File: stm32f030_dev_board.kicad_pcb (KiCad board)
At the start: 2 copper layers, 0 parts

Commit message: Started PCB layout and added net labels to schematic
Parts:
- added C1: 100n, Capacitor_SMD:C_0402_1005Metric_Pad0.74x0.62mm_HandSolder, F.Cu at (66.1, 77.5)
- added C10: 22u, Capacitor_Tantalum_SMD:CP_EIA-3216-18_Kemet-A_Pad1.58x1.35mm_HandSolder, F.Cu at (139.4, 82.2)
- added C11: 10n, Capacitor_SMD:C_0402_1005Metric_Pad0.74x0.62mm_HandSolder, F.Cu at (147.2, 95.7)
- added C12: 100n, Capacitor_SMD:C_0402_1005Metric_Pad0.74x0.62mm_HandSolder, F.Cu at (147.2, 97.7)
- added C13: 100n, Capacitor_SMD:C_0402_1005Metric_Pad0.74x0.62mm_HandSolder, F.Cu at (150.4, 89.8)
- added C14: 100n, Capacitor_SMD:C_0402_1005Metric_Pad0.74x0.62mm_HandSolder, F.Cu at (98.9, 140.1)
- added C15: 100n, Capacitor_SMD:C_0402_1005Metric_Pad0.74x0.62mm_HandSolder, F.Cu at (90.7, 136.5)
- added C16: 100n, Capacitor_SMD:C_0402_1005Metric_Pad0.74x0.62mm_HandSolder, F.Cu at (94.4, 128.2)
- added C17: 100n, Capacitor_SMD:C_0402_1005Metric_Pad0.74x0.62mm_HandSolder, F.Cu at (150.4, 97.7)
- added C18: 100n, Capacitor_SMD:C_0402_1005Metric_Pad0.74x0.62mm_HandSolder, F.Cu at (153.6, 89.8)
- added C19: 4.7u, Capacitor_Tantalum_SMD:CP_EIA-3216-18_Kemet-A_Pad1.58x1.35mm_HandSolder, F.Cu at (139.4, 85.4)
- added C2: 100n, Capacitor_SMD:C_0402_1005Metric_Pad0.74x0.62mm_HandSolder, F.Cu at (144.0, 91.8)
- added C20: 4.7u, Capacitor_Tantalum_SMD:CP_EIA-3216-18_Kemet-A_Pad1.58x1.35mm_HandSolder, F.Cu at (139.4, 88.5)
- added C21: 27p, Capacitor_SMD:C_0402_1005Metric_Pad0.74x0.62mm_HandSolder, F.Cu at (85.1, 130.4)
- added C22: 27p, Capacitor_SMD:C_0402_1005Metric_Pad0.74x0.62mm_HandSolder, F.Cu at (85.1, 133.9)
- added C23: 20p, Capacitor_SMD:C_0603_1608Metric_Pad1.08x0.95mm_HandSolder, F.Cu at (70.3, 93.2)
- added C24: 20p, Capacitor_SMD:C_0603_1608Metric_Pad1.08x0.95mm_HandSolder, F.Cu at (70.3, 97.8)
- added C25: 4.7u, Capacitor_Tantalum_SMD:CP_EIA-3216-18_Kemet-A_Pad1.58x1.35mm_HandSolder, F.Cu at (139.4, 91.7)
- added C26: 6p, Capacitor_SMD:C_0603_1608Metric_Pad1.08x0.95mm_HandSolder, F.Cu at (70.4, 82.3)
- added C27: 6p, Capacitor_SMD:C_0603_1608Metric_Pad1.08x0.95mm_HandSolder, F.Cu at (70.5, 86.0)
- added C28: 10u, Capacitor_Tantalum_SMD:CP_EIA-6032-28_Kemet-C_Pad2.25x2.35mm_HandSolder, F.Cu at (155.2, 73.7)
- added C29: 100n, Capacitor_SMD:C_0402_1005Metric_Pad0.74x0.62mm_HandSolder, F.Cu at (97.4, 128.2)
- added C3: 100n, Capacitor_SMD:C_0402_1005Metric_Pad0.74x0.62mm_HandSolder, F.Cu at (75.0, 82.8)
- added C30: 4.7u, Capacitor_Tantalum_SMD:CP_EIA-3216-18_Kemet-A_Pad1.58x1.35mm_HandSolder, F.Cu at (138.3, 99.3)
- added C4: 100n, Capacitor_SMD:C_0402_1005Metric_Pad0.74x0.62mm_HandSolder, F.Cu at (79.5, 94.6)
- added C5: 100n, Capacitor_SMD:C_0402_1005Metric_Pad0.74x0.62mm_HandSolder, F.Cu at (86.0, 94.6)
- added C6: 100n, Capacitor_SMD:C_0402_1005Metric_Pad0.74x0.62mm_HandSolder, F.Cu at (90.0, 83.6)
- added C7: 100n, Capacitor_SMD:C_0402_1005Metric_Pad0.74x0.62mm_HandSolder, F.Cu at (79.0, 79.7)
- added C8: 10n, Capacitor_SMD:C_0402_1005Metric_Pad0.74x0.62mm_HandSolder, F.Cu at (74.9, 89.2)
- added C9: 4.7u, Capacitor_Tantalum_SMD:CP_EIA-3216-18_Kemet-A_Pad1.58x1.35mm_HandSolder, F.Cu at (139.4, 79.1)
- added D1: RED, Capacitor_SMD:C_0402_1005Metric_Pad0.74x0.62mm_HandSolder, F.Cu at (153.6, 97.7)
- added J2: Conn_01x16, Connector_PinSocket_2.54mm:PinSocket_1x16_P2.54mm_Vertical, F.Cu at (21.0, 56.8)
- added J3: Conn_01x16, Connector_PinSocket_2.54mm:PinSocket_1x16_P2.54mm_Vertical, F.Cu at (26.8, 56.8)
- added J4: Conn_01x16, Connector_PinSocket_2.54mm:PinSocket_1x16_P2.54mm_Vertical, F.Cu at (35.7, 56.5)
- added J5: Conn_01x06, Connector_PinSocket_2.54mm:PinSocket_1x06_P2.54mm_Vertical, F.Cu at (47.5, 83.8)
- added J6: Conn_01x04, Connector_PinSocket_2.54mm:PinSocket_1x04_P2.54mm_Vertical, F.Cu at (48.3, 69.1)
- added J7: USB_C_Receptacle_USB2.0_16P, Connector_USB:USB_C_Receptacle_GCT_USB4105-xx-A_16P_TopMnt_Horizontal, F.Cu at (152.8, 104.0)
- added L1: 600R/0.5A, Inductor_SMD:L_1206_3216Metric_Pad1.22x1.90mm_HandSolder, F.Cu at (140.8, 71.4)
- added L2: 600R/0.5A, Inductor_SMD:L_1206_3216Metric_Pad1.22x1.90mm_HandSolder, F.Cu at (140.8, 74.9)
- added Q1: DMP3099L, Package_TO_SOT_SMD:SOT-23, F.Cu at (157.7, 91.2)
- added Q2: DMP3099L, Package_TO_SOT_SMD:SOT-23, F.Cu at (157.7, 95.9)
- added R10: 390, Resistor_SMD:R_0603_1608Metric_Pad0.98x0.95mm_HandSolder, F.Cu at (72.5, 97.8)
- added R11: 100k, Resistor_SMD:R_0603_1608Metric_Pad0.98x0.95mm_HandSolder, F.Cu at (134.2, 81.3)
- added R12: 100k, Resistor_SMD:R_0603_1608Metric_Pad0.98x0.95mm_HandSolder, F.Cu at (134.2, 83.8)
- added R13: 100, Resistor_SMD:R_0603_1608Metric_Pad0.98x0.95mm_HandSolder, F.Cu at (134.2, 86.3)
- added R2: 10k, Resistor_SMD:R_0603_1608Metric_Pad0.98x0.95mm_HandSolder, F.Cu at (125.5, 88.8)
- added R3: 5k1, Resistor_SMD:R_0603_1608Metric_Pad0.98x0.95mm_HandSolder, F.Cu at (125.5, 91.3)
- added R4: 5k1, Resistor_SMD:R_0603_1608Metric_Pad0.98x0.95mm_HandSolder, F.Cu at (129.8, 78.8)
- added R5: 22, Resistor_SMD:R_0603_1608Metric_Pad0.98x0.95mm_HandSolder, F.Cu at (86.3, 141.1)
- added R6: 22, Resistor_SMD:R_0603_1608Metric_Pad0.98x0.95mm_HandSolder, F.Cu at (86.3, 144.4)
- added R7: 12k, Resistor_SMD:R_0603_1608Metric_Pad0.98x0.95mm_HandSolder, F.Cu at (90.4, 133.0)
- added R8: 10k, Resistor_SMD:R_0603_1608Metric_Pad0.98x0.95mm_HandSolder, F.Cu at (102.9, 131.5)
- added R9: 10k, Resistor_SMD:R_0603_1608Metric_Pad0.98x0.95mm_HandSolder, F.Cu at (79.8, 75.3)
- added S1: EG1218, digikey-footprints:Switch_Slide_11.6x4mm_EG1218, F.Cu at (81.4, 71.8)
- added SW1: SW_Push, Button_Switch_THT:SW_PUSH_6mm_H5mm, F.Cu at (64.0, 75.4)
- added SW3: SW_Push, Button_Switch_THT:SW_PUSH_6mm_H5mm, F.Cu at (125.3, 103.1)
- added U1: STM32F030RCTx, Package_QFP:LQFP-64_10x10mm_P0.5mm, F.Cu at (82.5, 87.1)
- added U2: FT232H, Package_QFP:LQFP-48_7x7mm_P0.5mm, F.Cu at (96.6, 134.1)
- added U3: AMS1117-3.3, Package_TO_SOT_SMD:SOT-223-3_TabPin2, F.Cu at (155.6, 67.2)
- added Y1: 12MHz, Crystal:Crystal_HC49-4H_Vertical, F.Cu at (80.2, 129.6)
- added Y2: 8MHz, Crystal:Crystal_HC49-4H_Vertical, F.Cu at (66.0, 98.0)
- added Y3: 32.768kHz, Crystal:Crystal_SMD_Abracon_ABS25-4Pin_8.0x3.8mm, F.Cu at (64.7, 84.1)
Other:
- copper layers 2 -> 4

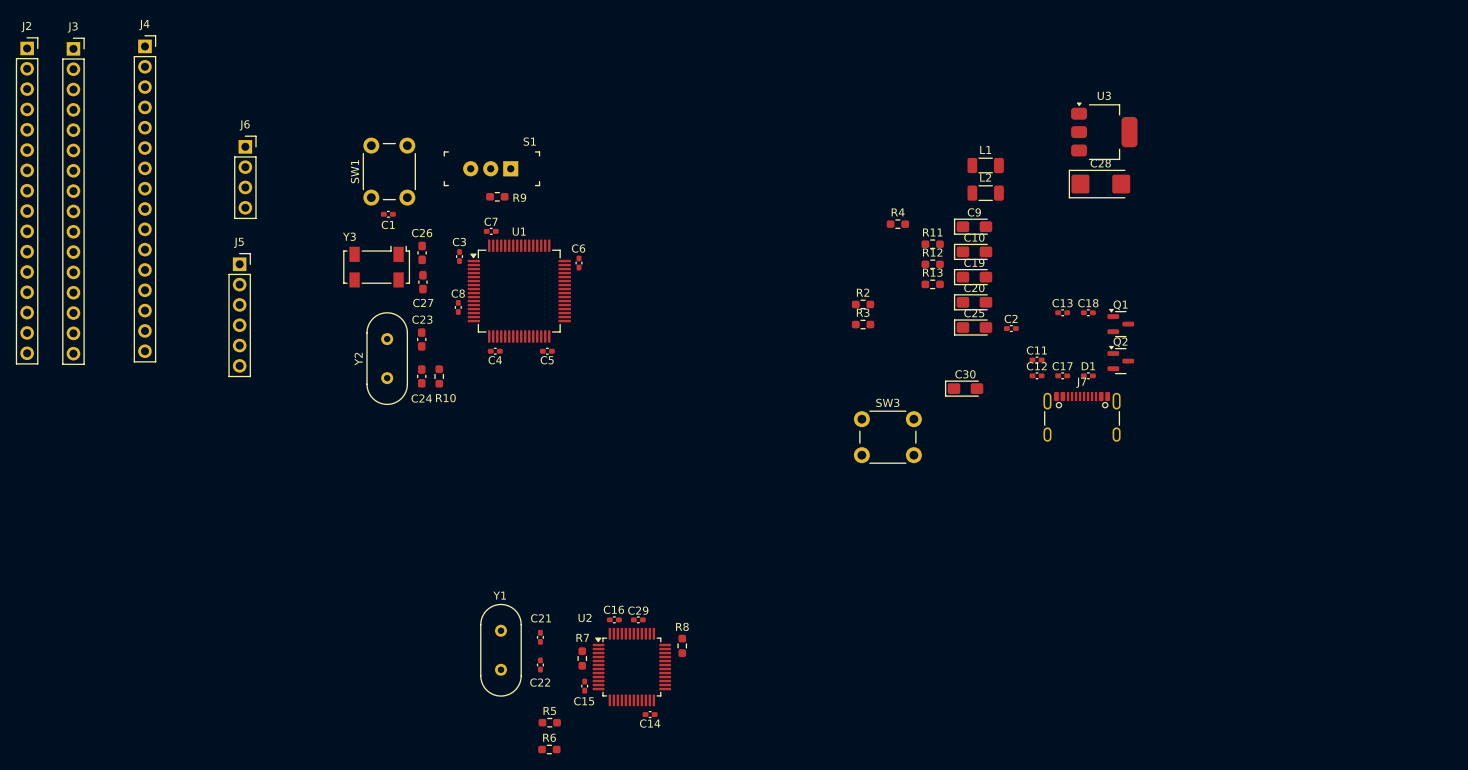
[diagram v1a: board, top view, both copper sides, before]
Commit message: Layout the pcb and added mounting holes to schematic and pcb
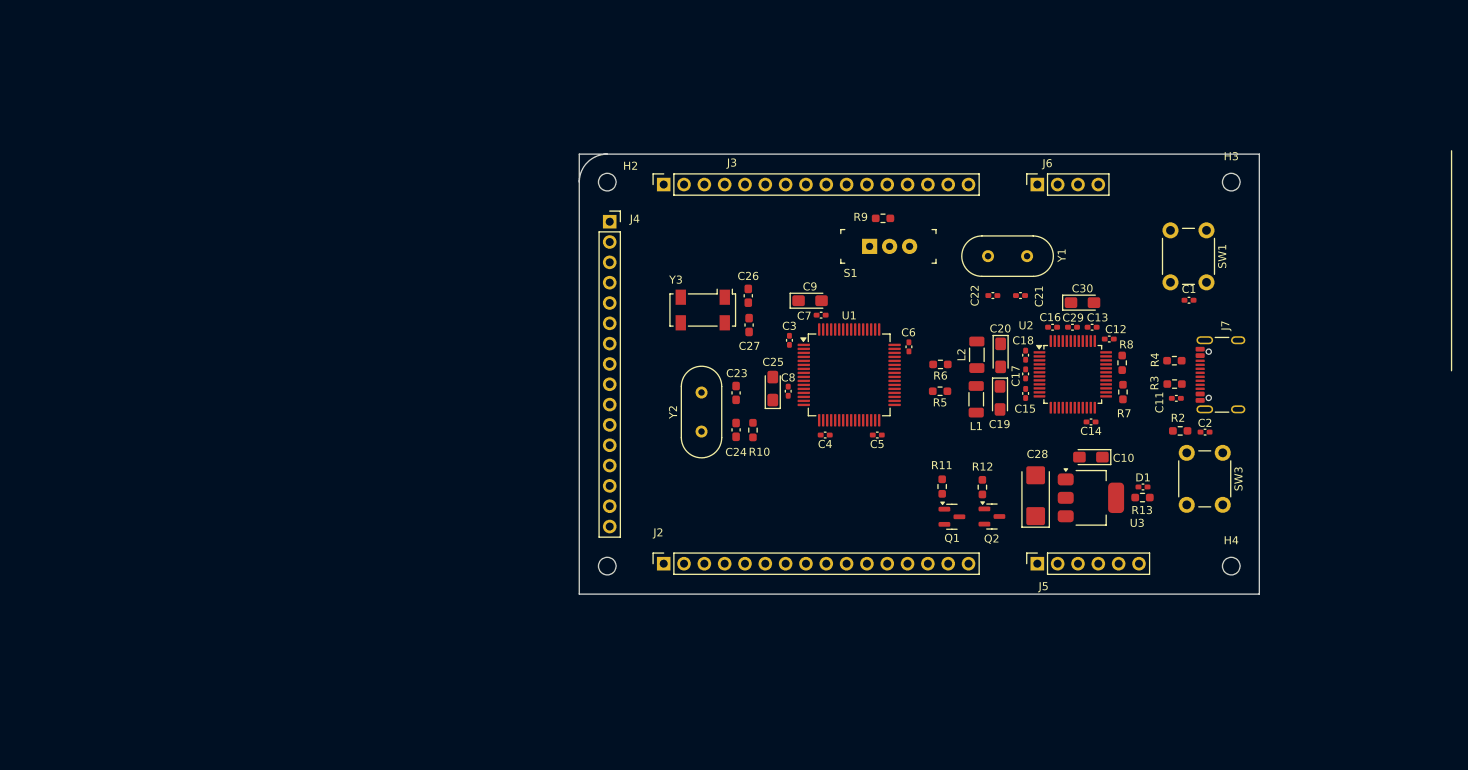
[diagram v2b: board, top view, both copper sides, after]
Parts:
- added H1: MountingHole, MountingHole:MountingHole_2.2mm_M2, F.Cu at (93.5, 121.5)
- added H2: MountingHole, MountingHole:MountingHole_2.2mm_M2, F.Cu at (93.5, 73.5)
- added H3: MountingHole, MountingHole:MountingHole_2.2mm_M2, F.Cu at (171.5, 73.5)
- added H4: MountingHole, MountingHole:MountingHole_2.2mm_M2, F.Cu at (171.5, 121.5)
- moved J5 106.5 mm to (147.3, 121.2), turned to 90 degrees
- moved SW1 104.5 mm to (168.4, 79.5), turned to -90 degrees
- moved J2 102.4 mm to (100.6, 121.2), turned to 90 degrees
- moved C1 100.7 mm to (166.2, 88.3), turned to 0 degrees
- moved J6 99.1 mm to (147.3, 73.8), turned to 90 degrees
- moved Y1 80.7 mm to (146.0, 82.8), turned to 180 degrees
- moved J3 75.7 mm to (100.6, 73.8), turned to 90 degrees
- moved R7 75.3 mm to (158.0, 99.7)
- moved C21 73.7 mm to (145.2, 87.7), turned to 0 degrees
- moved C22 73.0 mm to (141.7, 87.7), turned to 180 degrees
- moved R6 68.6 mm to (135.1, 96.3), turned to 180 degrees
- moved U2 66.1 mm to (151.7, 97.5)
- moved C14 66.1 mm to (154.0, 103.5)
- moved C15 66.1 mm to (145.8, 99.9)
- moved C16 65.9 mm to (149.2, 91.6)
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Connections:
- net Net-(D1-A) renamed /LED+
- net Net-(J7-CC1) renamed /CC1
- net Net-(J7-CC2) renamed /CC2
- net Net-(Q1-S) renamed /VI
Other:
- board outline added: 85 x 55 mm
